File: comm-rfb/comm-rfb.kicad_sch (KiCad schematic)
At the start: 6 parts, among them J1 PC104_Connector

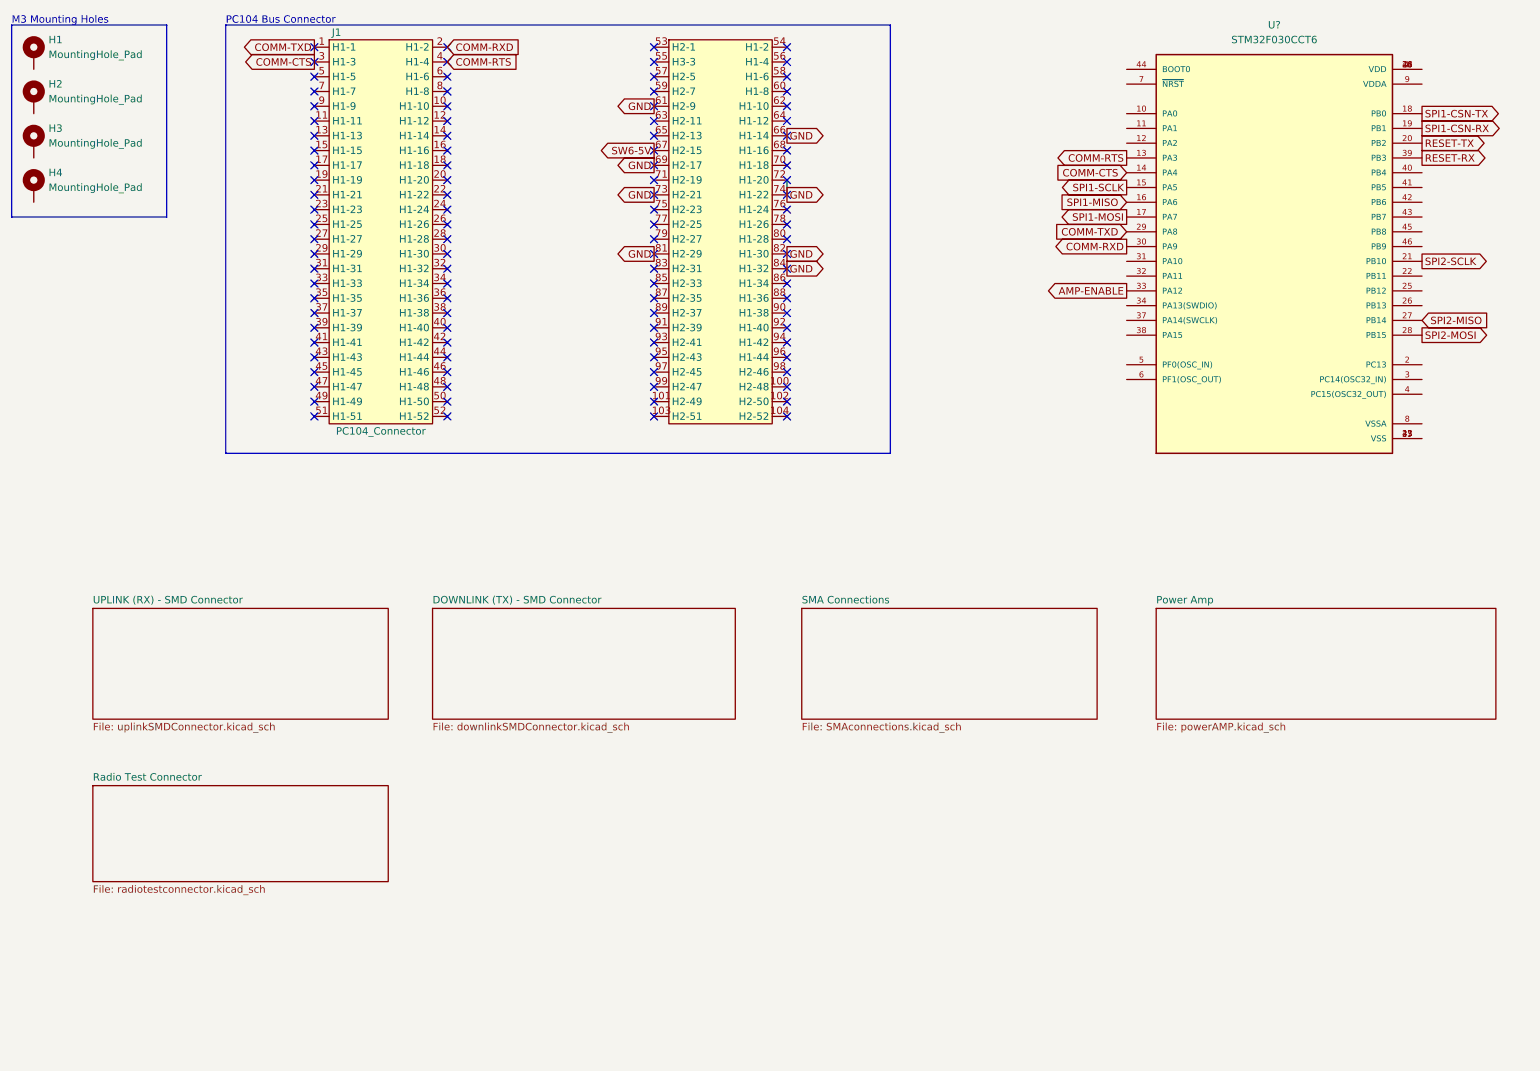
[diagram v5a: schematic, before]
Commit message: added test connectors and programming interfaces
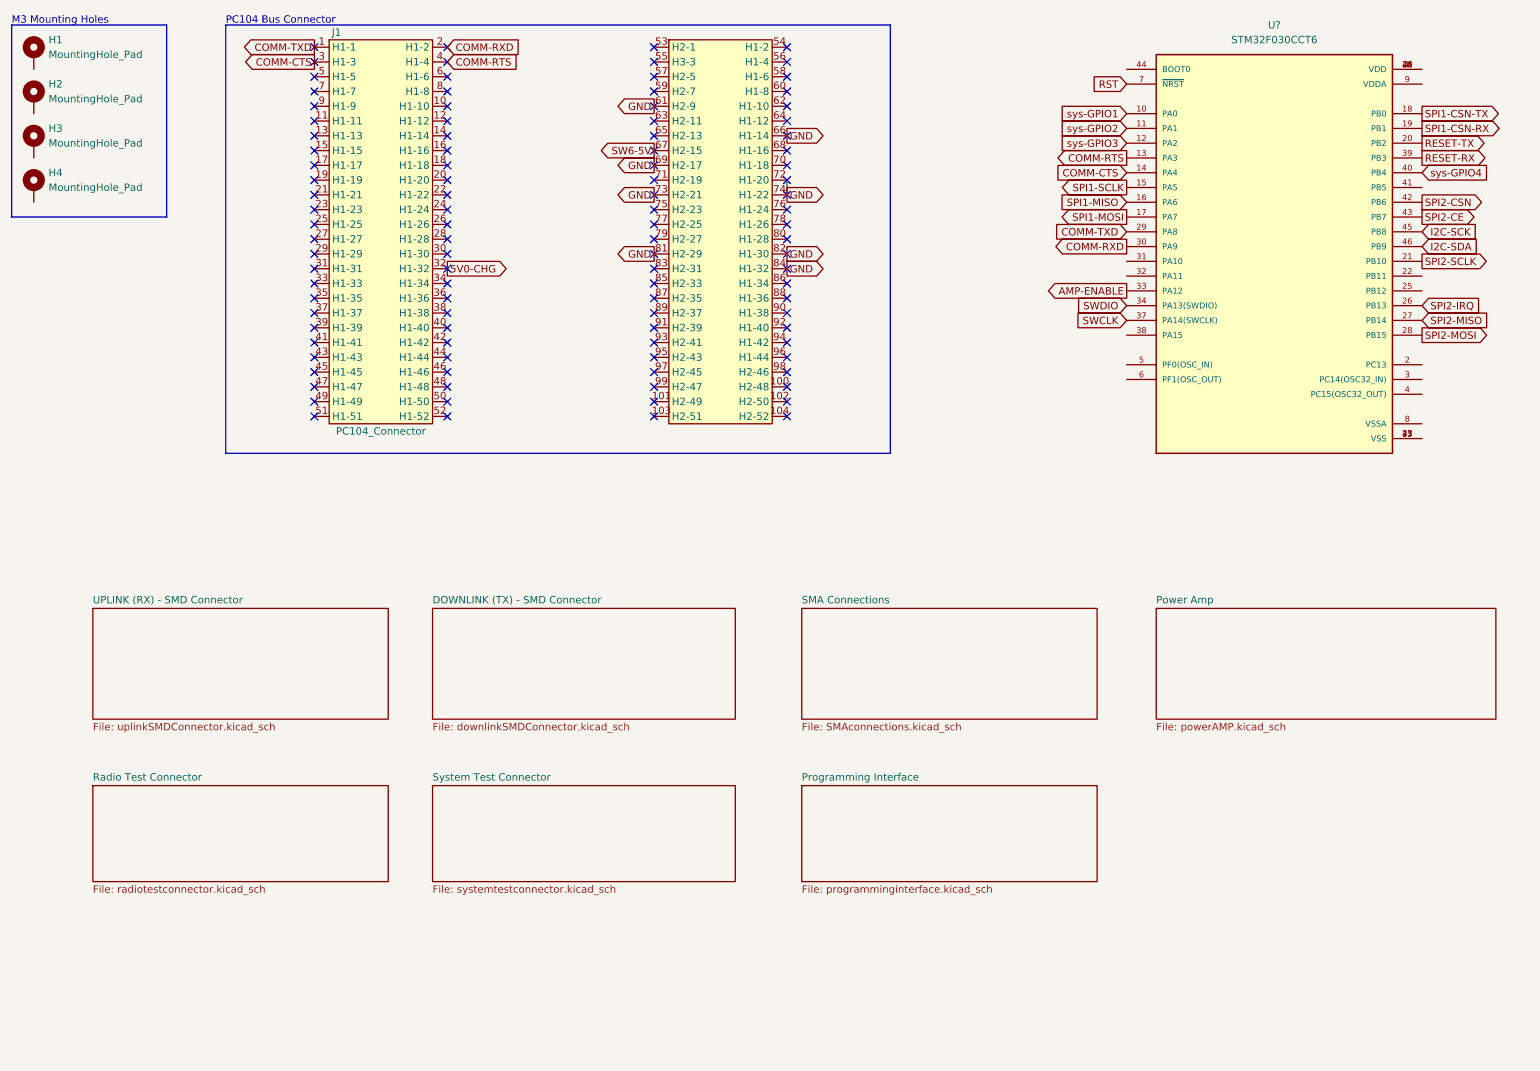
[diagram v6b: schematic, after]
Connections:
- net sys-GPIO1: now reaches U?.10 (PA0)
- net sys-GPIO2: now reaches U?.11 (PA1)
- net sys-GPIO3: now reaches U?.12 (PA2)
- net SPI2-IRQ: now reaches U?.26 (PB13)
- net SWDIO: now reaches U?.34 (PA13(SWDIO))
- net SWCLK: now reaches U?.37 (PA14(SWCLK))
- net sys-GPIO4: now reaches U?.40 (PB4)
- net SPI2-CSN: now reaches U?.42 (PB6)
- net SPI2-CE: now reaches U?.43 (PB7)
- net I2C-SCK: now reaches U?.45 (PB8)
- net I2C-SDA: now reaches U?.46 (PB9)
- net RST: now reaches U?.7 (~{NRST})
- net 5V0-CHG: now reaches J1.32 (H1-32)
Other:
- added sheet Programming Interface (programminginterface.kicad_sch)
- added sheet System Test Connector (systemtestconnector.kicad_sch)
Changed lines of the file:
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@@
+    )
+  )
+  (global_label "sys-GPIO4" (shape input) (at 256.54 40.64 0) (fields_autoplaced)
+    (effects (font (size 1.27 1.27)) (justify left))
+    (property "Intersheet References" "${INTERSHEET_REFS}" (id 0) (at 269.2341 40.5606 0)
+      (effects (font (size 1.27 1.27)) (justify left) hide)
     )
   )
@@
     )
   )
+  (global_label "SPI2-CSN" (shape output) (at 256.54 45.72 0) (fields_autoplaced)
+    (effects (font (size 1.27 1.27)) (justify left))
+    (property "Intersheet References" "${INTERSHEET_REFS}" (id 0) (at 268.6293 45.6406 0)
+      (effects (font (size 1.27 1.27)) (justify left) hide)
+    )
+  )
   (global_label "COMM-TXD" (shape input) (at 205.74 50.8 180) (fields_autoplaced)
     (effects (font (size 1.27 1.27)) (justify right))
@@
     )
   )
+  (global_label "RST" (shape input) (at 205.74 25.4 180) (fields_autoplaced)
+    (effects (font (size 1.27 1.27)) (justify right))
+    (property "Intersheet References" "${INTERSHEET_REFS}" (id 0) (at 199.8798 25.3206 0)
+      (effects (font (size 1.27 1.27)) (justify right) hide)
+    )
+  )
+  (global_label "5V0-CHG" (shape output) (at 88.9 57.15 0) (fields_autoplaced)
+    (effects (font (size 1.27 1.27)) (justify left))
+    (property "Intersheet References" "${INTERSHEET_REFS}" (id 0) (at 100.2636 57.0706 0)
+      (effects (font (size 1.27 1.27)) (justify left) hide)
+    )
+  )
   (global_label "COMM-RTS" (shape input) (at 88.9 21.59 0) (fields_autoplaced)
     (effects (font (size 1.27 1.27)) (justify left))
@@
     )
   )
+  (global_label "SPI2-CE" (shape output) (at 256.54 48.26 0) (fields_autoplaced)
+    (effects (font (size 1.27 1.27)) (justify left))
+    (property "Intersheet References" "${INTERSHEET_REFS}" (id 0) (at 267.2383 48.1806 0)
+      (effects (font (size 1.27 1.27)) (justify left) hide)
+    )
+  )
   (global_label "AMP-ENABLE" (shape output) (at 205.74 60.96 180) (fields_autoplaced)
     (effects (font (size 1.27 1.27)) (justify right))
@@
     )
   )
+  (global_label "sys-GPIO1" (shape input) (at 205.74 30.48 180) (fields_autoplaced)
+    (effects (font (size 1.27 1.27)) (justify right))
+    (property "Intersheet References" "${INTERSHEET_REFS}" (id 0) (at 193.0459 30.4006 0)
+      (effects (font (size 1.27 1.27)) (justify right) hide)
+    )
+  )
+  (global_label "SPI2-IRQ" (shape input) (at 256.54 63.5 0) (fields_autoplaced)
+    (effects (font (size 1.27 1.27)) (justify left))
+    (property "Intersheet References" "${INTERSHEET_REFS}" (id 0) (at 268.0245 63.4206 0)
+      (effects (font (size 1.27 1.27)) (justify left) hide)
+    )
+  )
   (global_label "SW6-5V" (shape output) (at 124.46 36.83 180) (fields_autoplaced)
     (effects (font (size 1.27 1.27)) (justify right))
@@
     )
   )
+  (global_label "I2C-SDA" (shape input) (at 256.54 53.34 0) (fields_autoplaced)
+    (effects (font (size 1.27 1.27)) (justify left))
+    (property "Intersheet References" "${INTERSHEET_REFS}" (id 0) (at 267.1779 53.2606 0)
+      (effects (font (size 1.27 1.27)) (justify left) hide)
+    )
+  )
+  (global_label "sys-GPIO2" (shape input) (at 205.74 33.02 180) (fields_autoplaced)
+    (effects (font (size 1.27 1.27)) (justify right))
+    (property "Intersheet References" "${INTERSHEET_REFS}" (id 0) (at 193.0459 32.9406 0)
+      (effects (font (size 1.27 1.27)) (justify right) hide)
+    )
+  )
   (global_label "COMM-RXD" (shape input) (at 88.9 19.05 0) (fields_autoplaced)
     (effects (font (size 1.27 1.27)) (justify left))
@@
     )
   )
+  (global_label "SWDIO" (shape input) (at 205.74 63.5 180) (fields_autoplaced)
+    (effects (font (size 1.27 1.27)) (justify right))
+    (property "Intersheet References" "${INTERSHEET_REFS}" (id 0) (at 197.4607 63.4206 0)
+      (effects (font (size 1.27 1.27)) (justify right) hide)
+    )
+  )
   (global_label "SPI1-MISO" (shape input) (at 205.74 45.72 180) (fields_autoplaced)
     (effects (font (size 1.27 1.27)) (justify right))
@@
     )
   )
+  (global_label "I2C-SCK" (shape input) (at 256.54 50.8 0) (fields_autoplaced)
+    (effects (font (size 1.27 1.27)) (justify left))
+    (property "Intersheet References" "${INTERSHEET_REFS}" (id 0) (at 267.3593 50.7206 0)
+      (effects (font (size 1.27 1.27)) (justify left) hide)
+    )
+  )
+  (global_label "SWCLK" (shape input) (at 205.74 66.04 180) (fields_autoplaced)
+    (effects (font (size 1.27 1.27)) (justify right))
+    (property "Intersheet References" "${INTERSHEET_REFS}" (id 0) (at 197.0979 65.9606 0)
+      (effects (font (size 1.27 1.27)) (justify right) hide)
+    )
+  )
   (global_label "COMM-CTS" (shape input) (at 205.74 40.64 180) (fields_autoplaced)
     (effects (font (size 1.27 1.27)) (justify right))
     (property "Intersheet References" "${INTERSHEET_REFS}" (id 0) (at 192.804 40.5606 0)
+      (effects (font (size 1.27 1.27)) (justify right) hide)
+    )
+  )
+  (global_label "sys-GPIO3" (shape input) (at 205.74 35.56 180) (fields_autoplaced)
+    (effects (font (size 1.27 1.27)) (justify right))
+    (property "Intersheet References" "${INTERSHEET_REFS}" (id 0) (at 193.0459 35.4806 0)
       (effects (font (size 1.27 1.27)) (justify right) hide)
     )
@@
     )
   )
+  (sheet (at 86.36 146.05) (size 52.07 16.51) (fields_autoplaced)
+    (stroke (width 0.1524) (type solid) (color 0 0 0 0))
+    (fill (color 0 0 0 0.0000))
+    (property "Sheet name" "System Test Connector" (id 0) (at 86.36 145.3384 0)
+      (effects (font (size 1.27 1.27)) (justify left bottom))
+    )
+    (property "Sheet file" "systemtestconnector.kicad_sch" (id 1) (at 86.36 163.1446 0)
+      (effects (font (size 1.27 1.27)) (justify left top))
+    )
+  )
   (sheet (at 86.36 115.57) (size 52.07 19.05) (fields_autoplaced)
     (stroke (width 0.1524) (type solid) (color 0 0 0 0))
@@
     )
     (property "Sheet file" "radiotestconnector.kicad_sch" (id 1) (at 27.94 163.1446 0)
+      (effects (font (size 1.27 1.27)) (justify left top))
+    )
+  )
+  (sheet (at 149.86 146.05) (size 50.8 16.51) (fields_autoplaced)
+    (stroke (width 0.1524) (type solid) (color 0 0 0 0))
+    (fill (color 0 0 0 0.0000))
+    (property "Sheet name" "Programming Interface" (id 0) (at 149.86 145.3384 0)
+      (effects (font (size 1.27 1.27)) (justify left bottom))
+    )
+    (property "Sheet file" "programminginterface.kicad_sch" (id 1) (at 149.86 163.1446 0)
       (effects (font (size 1.27 1.27)) (justify left top))
     )
@@
     (path "/692e9f18-86ea-4b4e-8432-aeb1e884c0b2" (page "5"))
     (path "/87e579cb-6bd6-444c-8886-91b899b8cce6" (page "6"))
+    (path "/18daa7fa-7378-4c58-aa8f-34599c628d11" (page "7"))
+    (path "/edc7eefe-12bb-4425-b51a-4d6eb34cbded" (page "8"))
   )
   (symbol_instances
@@
       (reference "J?") (unit 1) (value "Conn_Coaxial") (footprint "Connector_Coaxial:SMA_Amphenol_132134-10_Vertical")
     )
+    (path "/87e579cb-6bd6-444c-8886-91b899b8cce6/3ab71b4b-2400-4402-a427-b56190a77c9d"
+      (reference "J?") (unit 1) (value "Conn_02x04_Counter_Clockwise") (footprint "")
+    )
     (path "/1134daf0-036a-4c8a-b49c-c0c69387f2ca/48f9d1ea-ce9e-45a5-bd04-a4e73a5279ef"
       (reference "J?") (unit 1) (value "Conn_Coaxial") (footprint "Connector_Coaxial:SMA_Amphenol_132134-10_Vertical")
@@
       (reference "J?") (unit 1) (value "Conn_Coaxial") (footprint "Connector_Coaxial:SMA_Amphenol_132134-10_Vertical")
     )
+    (path "/edc7eefe-12bb-4425-b51a-4d6eb34cbded/8aef7173-100f-4685-9402-7ada21f71c63"
+      (reference "J?") (unit 1) (value "Conn_02x05_Counter_Clockwise") (footprint "")
+    )
+    (path "/18daa7fa-7378-4c58-aa8f-34599c628d11/985d0feb-1a43-4dd9-b270-3e22f5623ba4"
+      (reference "J?") (unit 1) (value "Conn_02x06_Odd_Even") (footprint "")
+    )
     (path "/75ea27b9-372e-4963-95b4-2f2bcb94e567/a2c994cc-ffa4-4456-ac7d-1924ce8dfac1"

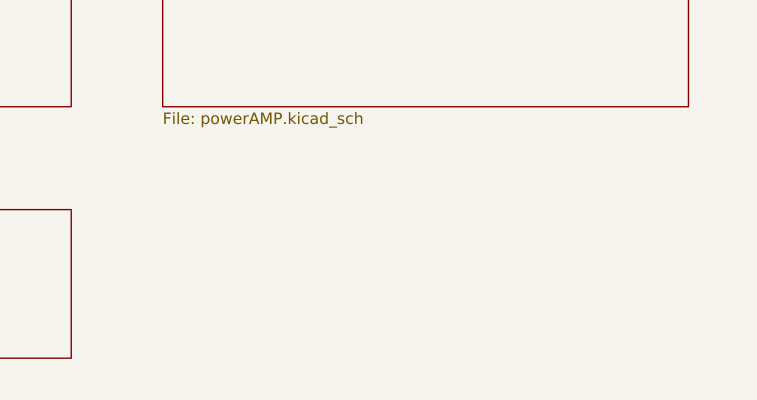
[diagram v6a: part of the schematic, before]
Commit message: added voltage converter schematic
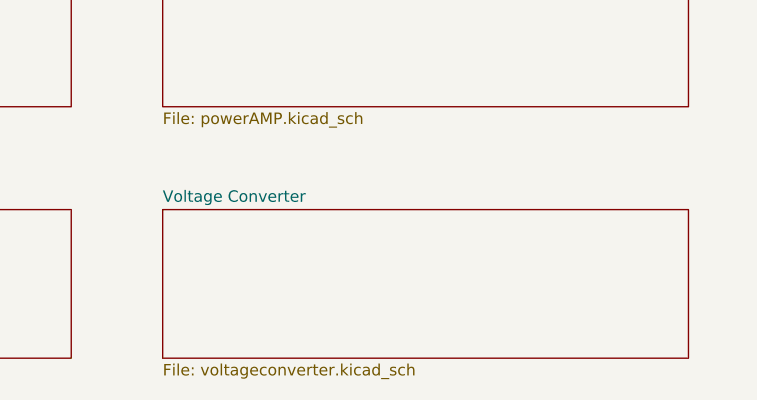
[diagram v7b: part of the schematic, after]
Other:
- added sheet Voltage Converter (voltageconverter.kicad_sch)
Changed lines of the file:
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@@
+    )
+  )
+  (sheet (at 210.82 146.05) (size 58.42 16.51) (fields_autoplaced)
+    (stroke (width 0.1524) (type solid) (color 0 0 0 0))
+    (fill (color 0 0 0 0.0000))
+    (property "Sheet name" "Voltage Converter" (id 0) (at 210.82 145.3384 0)
+      (effects (font (size 1.27 1.27)) (justify left bottom))
+    )
+    (property "Sheet file" "voltageconverter.kicad_sch" (id 1) (at 210.82 163.1446 0)
+      (effects (font (size 1.27 1.27)) (justify left top))
     )
   )
@@
     (path "/18daa7fa-7378-4c58-aa8f-34599c628d11" (page "7"))
     (path "/edc7eefe-12bb-4425-b51a-4d6eb34cbded" (page "8"))
+    (path "/c253291c-bb52-4e8f-af5c-cbf2e48e8d2a" (page "9"))
   )
   (symbol_instances
@@
       (reference "#PWR?") (unit 1) (value "GND") (footprint "")
     )
+    (path "/c253291c-bb52-4e8f-af5c-cbf2e48e8d2a/291a9e8b-063c-4500-b38a-f9143f0e90bb"
+      (reference "#PWR?") (unit 1) (value "GND") (footprint "")
+    )
     (path "/692e9f18-86ea-4b4e-8432-aeb1e884c0b2/3fc1f3ca-0173-43c5-a009-6e81b6f97b1f"
+      (reference "#PWR?") (unit 1) (value "GND") (footprint "")
+    )
+    (path "/c253291c-bb52-4e8f-af5c-cbf2e48e8d2a/54902a51-d053-41b4-abe1-d98fd92175fe"
       (reference "#PWR?") (unit 1) (value "GND") (footprint "")
     )
@@
       (reference "#PWR?") (unit 1) (value "GND") (footprint "")
     )
+    (path "/c253291c-bb52-4e8f-af5c-cbf2e48e8d2a/e6e2f4c9-0ea2-4453-90a7-9cf46925cdf8"
+      (reference "#PWR?") (unit 1) (value "GND") (footprint "")
+    )
+    (path "/c253291c-bb52-4e8f-af5c-cbf2e48e8d2a/e9376dba-e92c-4eb5-a170-ac3eb3869f10"
+      (reference "#PWR?") (unit 1) (value "GND") (footprint "")
+    )
     (path "/33e637d8-a37e-4c9b-b76e-8d40605182c6/ea33cf72-6549-4163-b5be-a9170e251995"
       (reference "#PWR?") (unit 1) (value "GND") (footprint "")
@@
     (path "/692e9f18-86ea-4b4e-8432-aeb1e884c0b2/2b4f2a19-5abc-496c-95d5-206b91f31acd"
       (reference "C?") (unit 1) (value "1000p") (footprint "")
+    )
+    (path "/c253291c-bb52-4e8f-af5c-cbf2e48e8d2a/2ee612b0-de7d-4ece-9f82-85f1df39d995"
+      (reference "C?") (unit 1) (value "10uF") (footprint "")
     )
     (path "/692e9f18-86ea-4b4e-8432-aeb1e884c0b2/5d87e782-851c-4f5f-bf93-d7123ab1bde8"
@@
     (path "/692e9f18-86ea-4b4e-8432-aeb1e884c0b2/cb37d10f-c63d-414c-a231-a60cf028d22e"
       (reference "C?") (unit 1) (value "10p") (footprint "")
+    )
+    (path "/c253291c-bb52-4e8f-af5c-cbf2e48e8d2a/ee3fc685-337f-45d3-84ea-5bed741e27b2"
+      (reference "C?") (unit 1) (value "22uF") (footprint "")
+    )
+    (path "/c253291c-bb52-4e8f-af5c-cbf2e48e8d2a/f65651ef-1724-41f6-84e6-7f18380e26ff"
+      (reference "D?") (unit 1) (value "10V") (footprint "Package_TO_SOT_SMD:SOT-23")
     )
     (path "/62767276-38ba-4eba-99b6-994ad2efc4aa"
@@
       (reference "L?") (unit 1) (value "22n") (footprint "")
     )
+    (path "/c253291c-bb52-4e8f-af5c-cbf2e48e8d2a/8ec10dba-fc5a-47b0-8738-9d7d7d45a930"
+      (reference "Q?") (unit 1) (value "Q_PMOS_DGS") (footprint "")
+    )
     (path "/692e9f18-86ea-4b4e-8432-aeb1e884c0b2/82515fb1-9eff-4a38-b8b7-126750192eb5"
       (reference "R?") (unit 1) (value "15") (footprint "")
@@
       (reference "R?") (unit 1) (value "330") (footprint "")
     )
+    (path "/c253291c-bb52-4e8f-af5c-cbf2e48e8d2a/a9db812e-169d-4fe3-86df-23b4fbde4d6a"
+      (reference "R?") (unit 1) (value "10k") (footprint "")
+    )
     (path "/692e9f18-86ea-4b4e-8432-aeb1e884c0b2/bae6c4e0-014f-4b31-94e4-7d32639e5820"
       (reference "R?") (unit 1) (value "9.1k") (footprint "")
     )
+    (path "/c253291c-bb52-4e8f-af5c-cbf2e48e8d2a/97014538-caec-4972-b3da-68a9c5abd210"
+      (reference "U?") (unit 1) (value "BU33SA5WGWZ-E2") (footprint "qsat5to3:BU33SA5WGWZ-E2")
+    )
     (path "/b80cbbdc-16b1-4161-95f2-05a8bd9b42d9"
